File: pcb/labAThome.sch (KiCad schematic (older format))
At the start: 69 parts, among them J1 I2C, J10 SRV2, J11 3.5.24.GND, J12 NEOPIXEL, J13 Barrel_Jack_Switch, J2 SRV1, J3 5V, J4 EXT, J5 VPS, J6 FAN3, J7 1wire, J8 1wire, J9 FAN1, K1 G5V-2, K2 G5V-2, K3 G5V-2, M1 HXJ8002_MODULE, M2 NEOPIXEL, M3 SN65HVD230_MODULE, Q1 IRLZ44N, Q2 IRLZ44N, Q3 IRLZ44N, Q5 2N3904, SW1 RED, SW2 GREEN, SW4 BLUE, SW5 WHITE, SW7 ROTENC, U1 SR602, U10 MAX3485_MODULE, U11 AM312, U2 24V->5V, U3 PDC004_Module, U4 ESP32_DEVKITC_COMPATIBLE, U5 LD06AJSA, U6 GY-302, U7 Display, U8 INMP441_Module, X1 FAN_6024

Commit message: PCB last version without SMD
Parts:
- added C2: u1, Capacitor_THT:C_Rect_L4.0mm_W2.5mm_P2.50mm, symbol Device:C
- added J14: Conn_Coaxial, Connector_Coaxial:SMA_Amphenol_132289_EdgeMount, symbol Connector:Conn_Coaxial
- added JP5: CLK_LORA, Jumper:SolderJumper-2_P1.3mm_Open_RoundedPad1.0x1.5mm, symbol Device:Jumper_NO_Small
- added JP6: MOSI_LORA, Jumper:SolderJumper-2_P1.3mm_Open_RoundedPad1.0x1.5mm, symbol Device:Jumper_NO_Small
- added JP8, JP9: I2C_SPI, Jumper:SolderJumper-3_P1.3mm_Open_RoundedPad1.0x1.5mm_NumberLabels, symbol Jumper:Jumper_3_Open
- added U9: RFM95W-868S2, RF_Module:HOPERF_RFM9XW_SMD, symbol RF_Module:RFM95W-868S2
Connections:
- net labels added: SPI_CLK, SPI_IO1, SPI_IO2, SPI_MISO, SPI_MOSI
- net labels removed: LCD_CLK, LCD_DC, LCD_MOSI, LCD_RES
- wire segments 127 -> 137
- no-connect marks 14 -> 19
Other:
- note added: "Extensions"
- note removed: "Gegenseitiger Ausschluss:\n- 1wire und Servo2\n- I2S und RS485\n- Relay 3 und Buzzer"
- note removed: "https://www.kriwanek.de/index.php/de/homeautomation/esp8266/368-tasten-per-analogeingang-abfragen"
- moved on the sheet: M3, U10, U7, U8

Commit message: PCB labathomev5 as ordered at jlcpcb
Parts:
- removed J12: NEOPIXEL, Connector_PinSocket_2.54mm:PinSocket_1x04_P2.54mm_Vertical, symbol Connector_Generic:Conn_01x04
- removed M2: NEOPIXEL, smopla:NEOPIXEL_STICK, symbol Mechanical:MountingHole
- removed Q1, Q3: IRLZ44N, Package_TO_SOT_THT:TO-220-3_Horizontal_TabDown, symbol Device:Q_NMOS_GDS
- removed Q5: 2N3904, Package_TO_SOT_THT:TO-92_HandSolder, symbol Transistor_BJT:2N3904
- added FID1: OSHW, Symbol:OSHW-Logo_5.7x6mm_SilkScreen, symbol Mechanical:Fiducial
- added FID3: NonCommercial, Symbol:Symbol_CC-Noncommercial_CopperTop_Small, symbol Mechanical:Fiducial
- added J12: NEOPIXEL, smopla:NEOPIXEL_STICK_alternativ, symbol Connector_Generic:Conn_02x04_Top_Bottom
- added J15: WS2812_OUT, Connector_PinHeader_2.54mm:PinHeader_1x04_P2.54mm_Vertical, symbol Connector_Generic:Conn_01x04
- added Q1, Q3: IRLML6344, Package_TO_SOT_SMD:SOT-23_Handsoldering, symbol Transistor_FET:IRLML0030
- added Q4: BC847, Package_TO_SOT_SMD:SOT-23_Handsoldering, symbol Transistor_BJT:BC847
- added m1: Attribution, Symbol:Symbol_CC-Attribution_CopperTop_Small, symbol Mechanical:Fiducial
- C1: footprint Capacitor_THT:CP_Radial_Tantal_D5.0mm_P5.00mm -> Capacitor_Tantalum_SMD:CP_EIA-3216-18_Kemet-A_Pad1.58x1.35mm_HandSolder
- C2: footprint Capacitor_THT:C_Rect_L4.0mm_W2.5mm_P2.50mm -> Capacitor_SMD:C_1206_3216Metric_Pad1.42x1.75mm_HandSolder
- D5: footprint Diode_THT:D_DO-41_SOD81_P7.62mm_Horizontal -> Diode_SMD:D_SMA_Handsoldering
- D8: footprint Diode_THT:D_DO-35_SOD27_P2.54mm_Vertical_AnodeUp -> Diode_SMD:D_SMA_Handsoldering
- J11: value 3.5.24.GND -> 24.5.GND.3
- J7, J8: footprint Connector_JST:JST_PH_B3B-PH-K_1x03_P2.00mm_Vertical -> Connector_JST:JST_XH_B3B-XH-A_1x03_P2.50mm_Vertical
- R1, R12, R13, R14, R15, R16, R18, R19, R2, R20, R21, R3, R4, R5, R7, R9: footprint Resistor_THT:R_Axial_DIN0207_L6.3mm_D2.5mm_P2.54mm_Vertical -> Resistor_SMD:R_1206_3216Metric_Pad1.42x1.75mm_HandSolder
- R10: footprint Resistor_THT:R_Axial_DIN0207_L6.3mm_D2.5mm_P7.62mm_Horizontal -> Resistor_SMD:R_1206_3216Metric_Pad1.42x1.75mm_HandSolder
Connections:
- net labels added: SPI_MOSIx
- wire segments 137 -> 140
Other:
- moved on the sheet: J14, JP2, JP3, JP5, JP6, U9

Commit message: Various big changes (sorry for beeing rude here...)
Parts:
- removed J4: EXT, Connector_JST:JST_XH_B5B-XH-AM_1x05_P2.50mm_Vertical, symbol Connector:Conn_01x05_Male
- added J4: EXT, Connector_JST:JST_XH_B6B-XH-A_1x06_P2.50mm_Vertical, symbol Connector_Generic:Conn_01x06
- J14: footprint Connector_Coaxial:SMA_Amphenol_132289_EdgeMount -> Connector_Coaxial:SMA_Samtec_SMA-J-P-X-ST-EM1_EdgeMount
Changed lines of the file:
@@
-	-1   0    0    -1
-$EndComp
-$Comp
-L Connector:Conn_01x05_Male J4
-U 1 1 5F35411A
-P 6500 4850
-F 0 "J4" H 6472 4874 50  0000 R CNN
-F 1 "EXT" H 6472 4783 50  0000 R CNN
-F 2 "Connector_JST:JST_XH_B5B-XH-AM_1x05_P2.50mm_Vertical" H 6500 4850 50  0001 C CNN
-F 3 "~" H 6500 4850 50  0001 C CNN
-	1    6500 4850
 	-1   0    0    -1
 $EndComp
@@
 F 0 "J14" H 5050 6325 50  0000 L CNN
 F 1 "Conn_Coaxial" H 5050 6234 50  0000 L CNN
-F 2 "Connector_Coaxial:SMA_Amphenol_132289_EdgeMount" H 4950 6350 50  0001 C CNN
+F 2 "Connector_Coaxial:SMA_Samtec_SMA-J-P-X-ST-EM1_EdgeMount" H 4950 6350 50  0001 C CNN
 F 3 " ~" H 4950 6350 50  0001 C CNN
 	1    4950 6350
@@
 	1    0    0    -1
 $EndComp
+$Comp
+L Connector_Generic:Conn_01x06 J4
+U 1 1 5F503E4B
+P 6500 4850
+F 0 "J4" H 6580 4842 50  0000 L CNN
+F 1 "EXT" H 6580 4751 50  0000 L CNN
+F 2 "Connector_JST:JST_XH_B6B-XH-A_1x06_P2.50mm_Vertical" H 6500 4850 50  0001 C CNN
+F 3 "~" H 6500 4850 50  0001 C CNN
+	1    6500 4850
+	1    0    0    -1
+$EndComp
+$Comp
+L power:+5V #PWR0136
+U 1 1 5F5053D4
+P 6300 5150
+F 0 "#PWR0136" H 6300 5000 50  0001 C CNN
+F 1 "+5V" V 6315 5278 50  0000 L CNN
+F 2 "" H 6300 5150 50  0001 C CNN
+F 3 "" H 6300 5150 50  0001 C CNN
+	1    6300 5150
+	0    -1   -1   0
+$EndComp
 $EndSCHEMATC

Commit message: labathome - first break through - simple and/or/rs working :-)
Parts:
- RV1: footprint Potentiometer_THT:Potentiometer_Runtron_RM-065_Vertical -> Potentiometer_THT:Potentiometer_Alps_RK09K_Single_Vertical
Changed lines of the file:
@@
 F 0 "RV1" H 1231 5004 50  0000 R CNN
 F 1 "10k" H 1231 5095 50  0000 R CNN
-F 2 "Potentiometer_THT:Potentiometer_Runtron_RM-065_Vertical" H 1300 5050 50  0001 C CNN
+F 2 "Potentiometer_THT:Potentiometer_Alps_RK09K_Single_Vertical" H 1300 5050 50  0001 C CNN
 F 3 "~" H 1300 5050 50  0001 C CNN
 	1    1300 5050

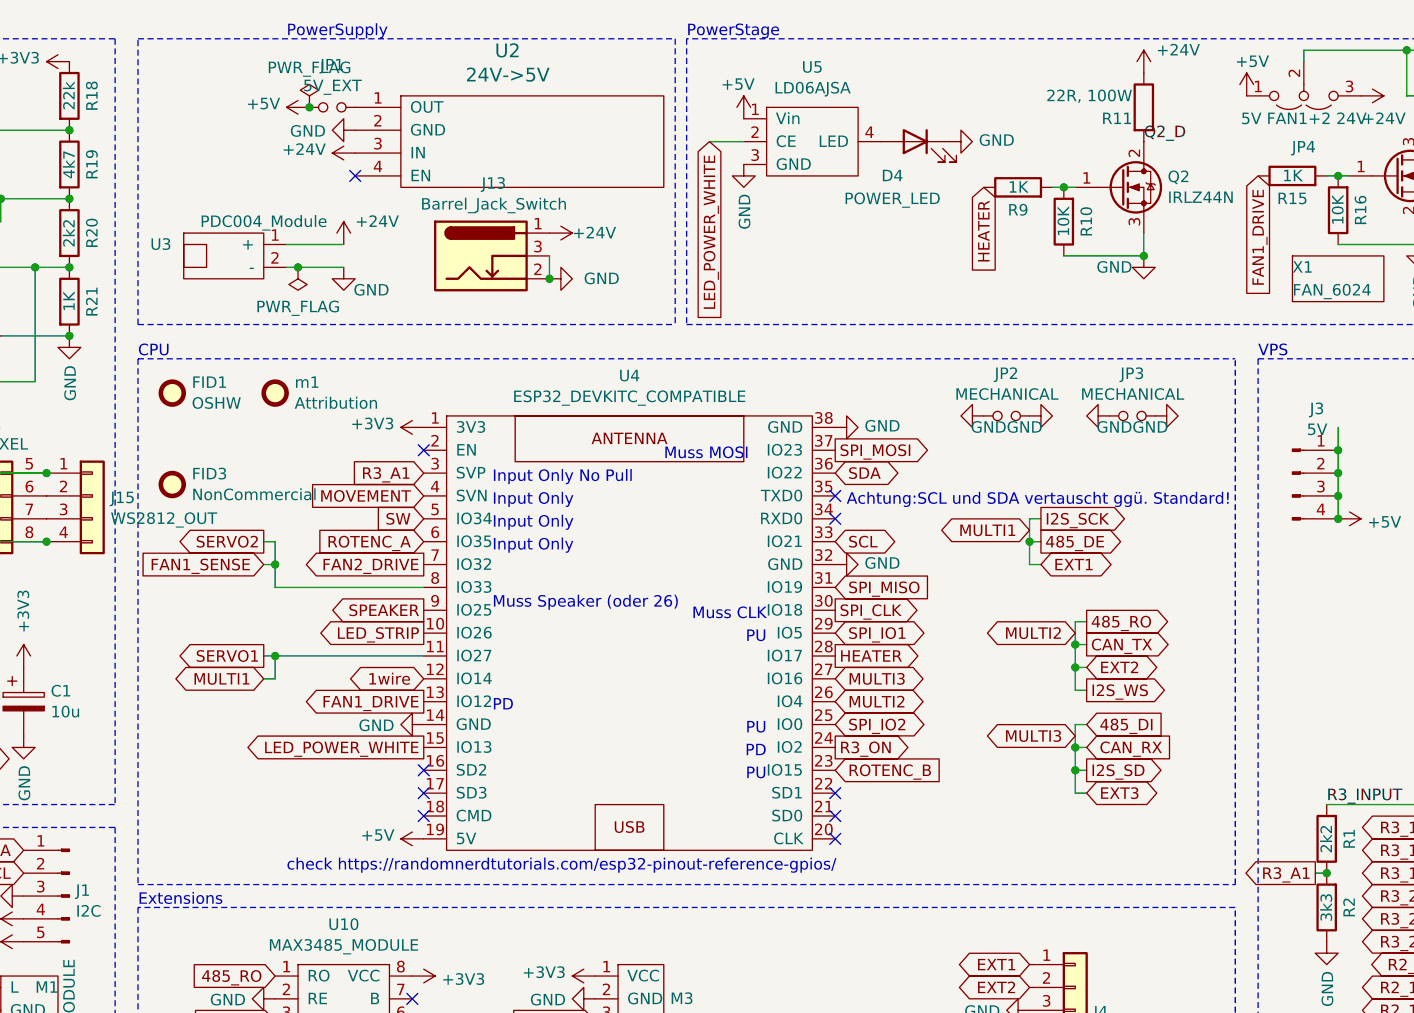
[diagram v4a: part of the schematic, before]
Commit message: Working experiment UI
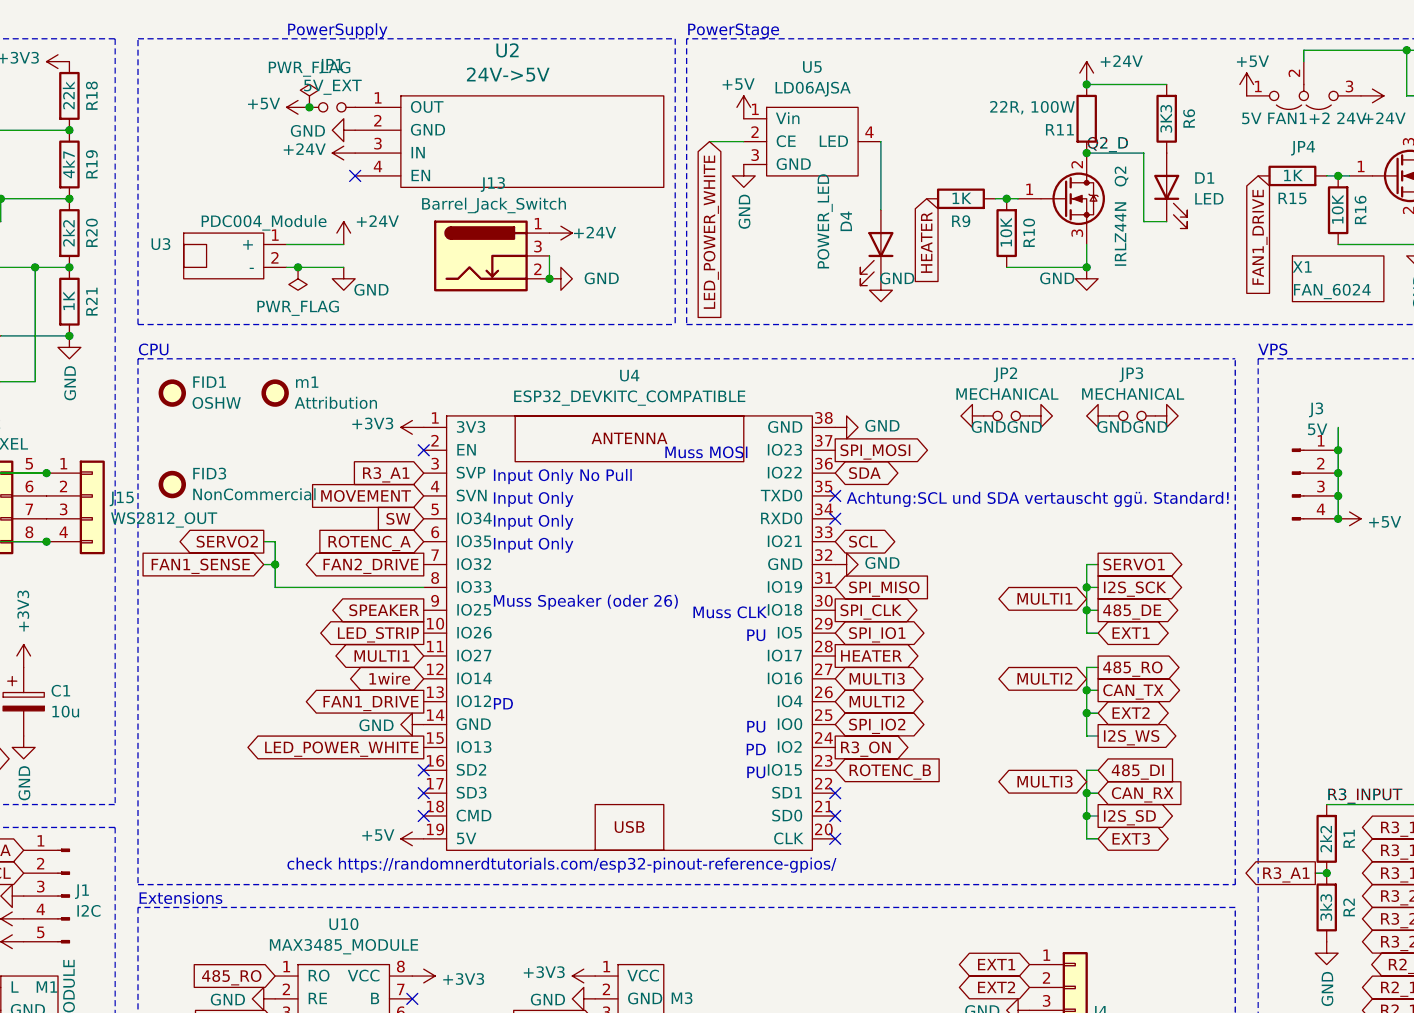
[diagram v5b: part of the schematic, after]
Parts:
- added D1: LED, LED_SMD:LED_0805_2012Metric_Pad1.15x1.40mm_HandSolder, symbol Device:LED
- added R6: 3K3, Resistor_SMD:R_1206_3216Metric_Pad1.42x1.75mm_HandSolder, symbol Device:R
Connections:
- wire segments 140 -> 143
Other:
- moved on the sheet: D4, Q2, R10, R11, R9
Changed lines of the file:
@@
 L Device:LED D4
 U 1 1 5E96EA71
-P 5800 1050
-F 0 "D4" H 5900 900 50  0000 C CNN
-F 1 "POWER_LED" H 5900 800 50  0000 C CNN
-F 2 "smopla:3W_LED" H 5800 1050 50  0001 C CNN
-F 3 "~" H 5800 1050 50  0001 C CNN
-	1    5800 1050
-	-1   0    0    -1
+P 5650 1500
+F 0 "D4" H 5750 1350 50  0000 C CNN
+F 1 "POWER_LED" H 5750 1250 50  0000 C CNN
+F 2 "smopla:3W_LED" H 5650 1500 50  0001 C CNN
+F 3 "~" H 5650 1500 50  0001 C CNN
+	1    5650 1500
+	0    1    -1   0
 $EndComp
 $Comp
 L Device:Q_NMOS_GDS Q2
 U 1 1 5E971BB2
-P 6700 1250
-F 0 "Q2" H 6904 1296 50  0000 L CNN
-F 1 "IRLZ44N" H 6904 1205 50  0000 L CNN
-F 2 "Package_TO_SOT_THT:TO-220-3_Horizontal_TabDown" H 6900 1350 50  0001 C CNN
-F 3 "~" H 6700 1250 50  0001 C CNN
-	1    6700 1250
+P 6450 1300
+F 0 "Q2" V 6700 1350 50  0000 L CNN
+F 1 "IRLZ44N" V 6700 1000 50  0000 L CNN
+F 2 "Package_TO_SOT_THT:TO-220-3_Horizontal_TabDown" H 6650 1400 50  0001 C CNN
+F 3 "~" H 6450 1300 50  0001 C CNN
+	1    6450 1300
 	1    0    0    -1
 $EndComp
@@
 L Device:R R11
 U 1 1 5E976325
-P 6800 900
-F 0 "R11" H 6750 850 50  0000 R CNN
-F 1 "22R, 100W" H 6750 950 50  0000 R CNN
-F 2 "smopla:Resistor_100W" V 6730 900 50  0001 C CNN
-F 3 "~" H 6800 900 50  0001 C CNN
-	1    6800 900
+P 6550 950
+F 0 "R11" H 6500 900 50  0000 R CNN
+F 1 "22R, 100W" H 6500 1000 50  0000 R CNN
+F 2 "smopla:Resistor_100W" V 6480 950 50  0001 C CNN
+F 3 "~" H 6550 950 50  0001 C CNN
+	1    6550 950
 	1    0    0    -1
 $EndComp
@@
 L power:GND #PWR022
 U 1 1 5EA42D94
-P 6800 1550
-F 0 "#PWR022" H 6800 1300 50  0001 C CNN
-F 1 "GND" H 6750 1500 50  0000 R CNN
-F 2 "" H 6800 1550 50  0001 C CNN
-F 3 "" H 6800 1550 50  0001 C CNN
-	1    6800 1550
+P 6550 1600
+F 0 "#PWR022" H 6550 1350 50  0001 C CNN
+F 1 "GND" H 6500 1550 50  0000 R CNN
+F 2 "" H 6550 1600 50  0001 C CNN
+F 3 "" H 6550 1600 50  0001 C CNN
+	1    6550 1600
 	1    0    0    -1
 $EndComp
@@
 L Device:R R10
 U 1 1 5EA43675
-P 6450 1400
-F 0 "R10" V 6350 1400 50  0000 C CNN
-F 1 "10K" V 6450 1400 50  0000 C CNN
-F 2 "Resistor_SMD:R_1206_3216Metric_Pad1.42x1.75mm_HandSolder" V 6380 1400 50  0001 C CNN
-F 3 "~" H 6450 1400 50  0001 C CNN
-	1    6450 1400
+P 6200 1450
+F 0 "R10" V 6100 1450 50  0000 C CNN
+F 1 "10K" V 6200 1450 50  0000 C CNN
+F 2 "Resistor_SMD:R_1206_3216Metric_Pad1.42x1.75mm_HandSolder" V 6130 1450 50  0001 C CNN
+F 3 "~" H 6200 1450 50  0001 C CNN
+	1    6200 1450
 	-1   0    0    1
 $EndComp
@@
 L Device:R R9
 U 1 1 5EA446FA
-P 6250 1250
-F 0 "R9" V 6150 1250 50  0000 C CNN
-F 1 "1K" V 6250 1250 50  0000 C CNN
-F 2 "Resistor_SMD:R_1206_3216Metric_Pad1.42x1.75mm_HandSolder" V 6180 1250 50  0001 C CNN
-F 3 "~" H 6250 1250 50  0001 C CNN
-	1    6250 1250
-	0    -1   -1   0
-$EndComp
-Wire Wire Line
-	6450 1550 6800 1550
-Wire Wire Line
-	6800 1550 6800 1450
-Connection ~ 6800 1550
-Wire Wire Line
-	6500 1250 6450 1250
-Wire Wire Line
-	6400 1250 6450 1250
-Connection ~ 6450 1250
-Text GLabel 6100 1250 3    50   Input ~ 0
+P 6000 1300
+F 0 "R9" V 5900 1300 50  0000 C CNN
+F 1 "1K" V 6000 1300 50  0000 C CNN
+F 2 "Resistor_SMD:R_1206_3216Metric_Pad1.42x1.75mm_HandSolder" V 5930 1300 50  0001 C CNN
+F 3 "~" H 6000 1300 50  0001 C CNN
+	1    6000 1300
+	0    -1   -1   0
+$EndComp
+Wire Wire Line
+	6200 1600 6550 1600
+Wire Wire Line
+	6550 1600 6550 1500
+Connection ~ 6550 1600
+Wire Wire Line
+	6250 1300 6200 1300
+Wire Wire Line
+	6150 1300 6200 1300
+Connection ~ 6200 1300
+Text GLabel 5850 1300 3    50   Input ~ 0
 HEATER
 $Comp
@@
 Text Notes 2400 2000 0    50   ~ 0
 CPU
-Text Label 6800 1050 0    50   ~ 0
+Text Label 6550 1100 0    50   ~ 0
 Q2_D
 $Comp
@@
 L power:GND #PWR0106
 U 1 1 5EC56799
-P 5950 1050
-F 0 "#PWR0106" H 5950 800 50  0001 C CNN
-F 1 "GND" V 5955 922 50  0000 R CNN
-F 2 "" H 5950 1050 50  0001 C CNN
-F 3 "" H 5950 1050 50  0001 C CNN
-	1    5950 1050
-	0    -1   -1   0
+P 5650 1650
+F 0 "#PWR0106" H 5650 1400 50  0001 C CNN
+F 1 "GND" H 5800 1650 50  0000 R CNN
+F 2 "" H 5650 1650 50  0001 C CNN
+F 3 "" H 5650 1650 50  0001 C CNN
+	1    5650 1650
+	1    0    0    -1
 $EndComp
 $Comp
@@
 Text Notes 3950 2850 0    50   ~ 0
 Input Only
-Text GLabel 2950 3300 0    50   Output ~ 0
+Text GLabel 6600 2900 2    50   Output ~ 0
 SERVO1
 Wire Wire Line
@@
 Text GLabel 1550 6400 2    50   Input ~ 0
 I2S_SD
-Text GLabel 6350 2700 2    50   Output ~ 0
+Text GLabel 6600 3000 2    50   Output ~ 0
 I2S_SCK
-Text GLabel 6550 3450 2    50   Output ~ 0
+Text GLabel 6600 3650 2    50   Output ~ 0
 I2S_WS
-Text GLabel 6550 3800 2    50   Output ~ 0
+Text GLabel 6600 4000 2    50   Output ~ 0
 I2S_SD
 Wire Wire Line
@@
 L power:+24V #PWR020
 U 1 1 5EE5F7E7
-P 6800 750
-F 0 "#PWR020" H 6800 600 50  0001 C CNN
-F 1 "+24V" H 6950 850 50  0000 C CNN
-F 2 "" H 6800 750 50  0001 C CNN
-F 3 "" H 6800 750 50  0001 C CNN
-	1    6800 750
+P 6550 800
+F 0 "#PWR020" H 6550 650 50  0001 C CNN
+F 1 "+24V" H 6700 900 50  0000 C CNN
+F 2 "" H 6550 800 50  0001 C CNN
+F 3 "" H 6550 800 50  0001 C CNN
+	1    6550 800
 	1    0    0    -1
 $EndComp
@@
 Text GLabel 5450 3500 2    50   BiDi ~ 0
 MULTI2
-Text GLabel 6550 3150 2    50   Output ~ 0
+Text GLabel 6600 3350 2    50   Output ~ 0
 485_RO
-Text GLabel 6300 2750 0    50   BiDi ~ 0
+Text GLabel 6550 3050 0    50   BiDi ~ 0
 MULTI1
 Wire Wire Line
-	6300 2700 6350 2700
-Wire Wire Line
-	6300 2800 6350 2800
-Wire Wire Line
-	6300 2700 6300 2800
-Text GLabel 6350 2800 2    50   Output ~ 0
+	6550 3100 6600 3100
+Wire Wire Line
+	6550 3000 6550 3100
+Text GLabel 6600 3100 2    50   Output ~ 0
 485_DE
-Text GLabel 6550 3600 2    50   Input ~ 0
+Text GLabel 6600 3800 2    50   Input ~ 0
 485_DI
-Text GLabel 6500 3200 0    50   BiDi ~ 0
+Text GLabel 6550 3400 0    50   BiDi ~ 0
 MULTI2
 Wire Wire Line
-	6500 3150 6550 3150
-Wire Wire Line
-	6500 3250 6550 3250
-Wire Wire Line
-	6500 3150 6500 3250
-Text GLabel 6500 3650 0    50   BiDi ~ 0
+	6550 3350 6600 3350
+Wire Wire Line
+	6550 3450 6600 3450
+Wire Wire Line
+	6550 3350 6550 3450
+Text GLabel 6550 3850 0    50   BiDi ~ 0
 MULTI3
 Wire Wire Line
-	6500 3600 6550 3600
-Wire Wire Line
-	6500 3700 6550 3700
-Wire Wire Line
-	6500 3600 6500 3700
-Text GLabel 6350 2900 2    50   BiDi ~ 0
+	6550 3800 6600 3800
+Wire Wire Line
+	6550 3900 6600 3900
+Wire Wire Line
+	6550 3800 6550 3900
+Text GLabel 6600 3200 2    50   BiDi ~ 0
 EXT1
 Wire Wire Line
-	6350 2900 6300 2900
-Wire Wire Line
-	6300 2900 6300 2800
-Connection ~ 6300 2800
-Text GLabel 6550 3350 2    50   BiDi ~ 0
+	6600 3200 6550 3200
+Wire Wire Line
+	6550 3200 6550 3100
+Connection ~ 6550 3100
+Text GLabel 6600 3550 2    50   BiDi ~ 0
 EXT2
-Text GLabel 6550 3900 2    50   BiDi ~ 0
+Text GLabel 6600 4100 2    50   BiDi ~ 0
 EXT3
 Wire Wire Line
-	6500 3250 6500 3350
-Wire Wire Line
-	6500 3350 6550 3350
-Connection ~ 6500 3250
-Wire Wire Line
-	6500 3700 6500 3800
-Wire Wire Line
-	6500 3800 6550 3800
-Connection ~ 6500 3700
+	6550 3450 6550 3550
+Wire Wire Line
+	6550 3550 6600 3550
+Connection ~ 6550 3450
+Wire Wire Line
+	6550 3900 6550 4000
+Wire Wire Line
+	6550 4000 6600 4000
+Connection ~ 6550 3900
 $Comp
 L Connector:Conn_01x05_Male J1
@@
 	0    1    1    0
 $EndComp
-Text GLabel 6550 3250 2    50   Output ~ 0
+Text GLabel 6600 3450 2    50   Output ~ 0
 CAN_TX
-Text GLabel 6550 3700 2    50   Input ~ 0
+Text GLabel 6600 3900 2    50   Input ~ 0
 CAN_RX
 Wire Wire Line
-	6500 3350 6500 3450
-Wire Wire Line
-	6500 3450 6550 3450
-Connection ~ 6500 3350
+	6550 3550 6550 3650
+Wire Wire Line
+	6550 3650 6600 3650
+Connection ~ 6550 3550
 Text GLabel 4400 4900 0    50   Input ~ 0
 CAN_TX
@@
 Text GLabel 4750 6950 2    50   Input ~ 0
 SPI_IO1
-Text GLabel 2950 3400 0    50   BiDi ~ 0
+Text GLabel 3650 3300 0    50   BiDi ~ 0
 MULTI1
-Wire Wire Line
-	3650 3300 3000 3300
-Wire Wire Line
-	2950 3400 3000 3400
-Wire Wire Line
-	3000 3400 3000 3300
-Connection ~ 3000 3300
-Wire Wire Line
-	3000 3300 2950 3300
 $Comp
 L Device:Jumper_NO_Small JP5
@@
 Connection ~ 2000 2800
 Wire Wire Line
-	6500 3800 6500 3900
-Wire Wire Line
-	6500 3900 6550 3900
-Connection ~ 6500 3800
+	6550 4000 6550 4100
+Wire Wire Line
+	6550 4100 6600 4100
+Connection ~ 6550 4000
 $Comp
 L Mechanical:Fiducial FID1
@@
 	0    -1   -1   0
 $EndComp
+Wire Wire Line
+	6600 3000 6550 3000
+Wire Wire Line
+	6550 3000 6550 2900
+Wire Wire Line
+	6550 2900 6600 2900
+Connection ~ 6550 3000
+$Comp
+L Device:R R6
+U 1 1 5F72B804
+P 6900 950
+F 0 "R6" V 6800 950 50  0000 C CNN
+F 1 "3K3" V 6900 950 50  0000 C CNN
+F 2 "Resistor_SMD:R_1206_3216Metric_Pad1.42x1.75mm_HandSolder" V 6830 950 50  0001 C CNN
+F 3 "~" H 6900 950 50  0001 C CNN
+	1    6900 950
+	-1   0    0    1
+$EndComp
+Wire Wire Line
+	5650 1050 5650 1350
+$Comp
+L Device:LED D1
+U 1 1 5F741B7D
+P 6900 1250
+F 0 "D1" V 6939 1132 50  0000 R CNN
+F 1 "LED" V 6848 1132 50  0000 R CNN
+F 2 "LED_SMD:LED_0805_2012Metric_Pad1.15x1.40mm_HandSolder" H 6900 1250 50  0001 C CNN
+F 3 "~" H 6900 1250 50  0001 C CNN
+	1    6900 1250
+	0    -1   -1   0
+$EndComp
+Wire Wire Line
+	6900 800  6550 800
+Connection ~ 6550 800
+Wire Wire Line
+	6800 1400 6900 1400
+Wire Wire Line
+	6550 1100 6800 1100
+Wire Wire Line
+	6800 1100 6800 1400
+Connection ~ 6550 1100
 $EndSCHEMATC
